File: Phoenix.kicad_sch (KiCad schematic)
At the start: 2 parts

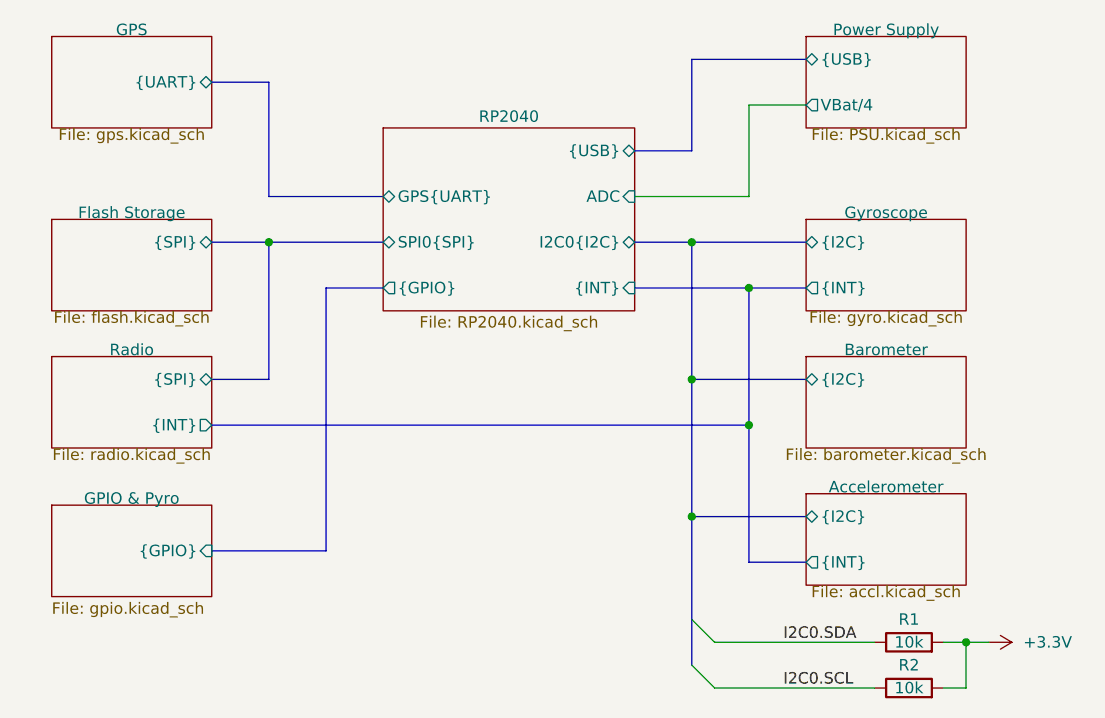
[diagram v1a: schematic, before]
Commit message: Connected the sensors, flash chip, Need to connect the radio and GPS
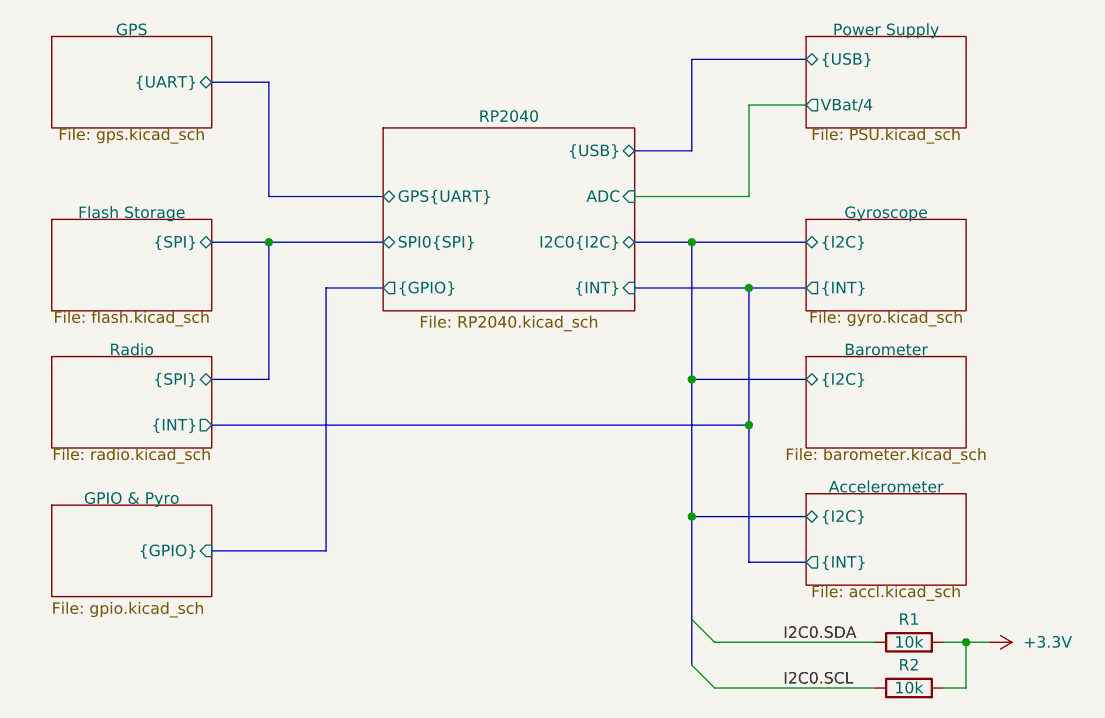
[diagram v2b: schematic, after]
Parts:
- R1, R2: footprint (none) -> Resistor_SMD:R_0603_1608Metric

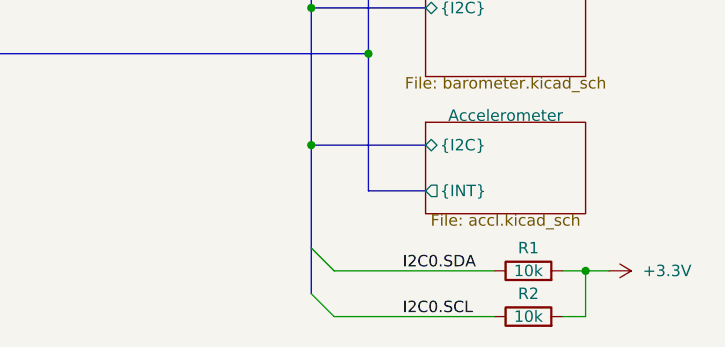
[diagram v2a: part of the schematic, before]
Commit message: Rearranged IO pins to make routing easier. Removed reset, changed BOOTSEL to button
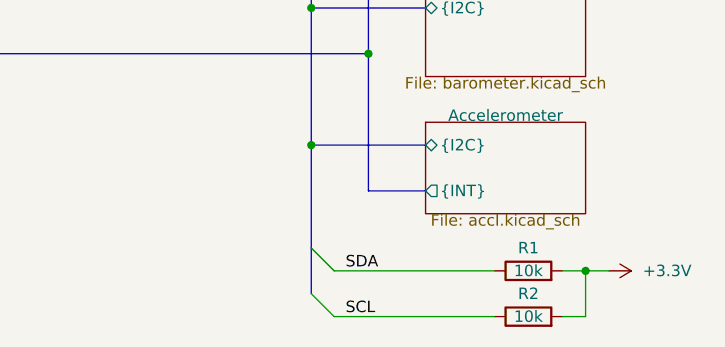
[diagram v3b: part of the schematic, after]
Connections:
- net I2C0.SCL renamed SCL
- net I2C0.SDA renamed SDA
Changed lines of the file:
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@@
   (junction (at 153.67 104.14) (diameter 0) (color 0 0 0 0)
   )
-  (bus_entry (at 125.73 104.14) (size -2.54 -2.54)
-    (stroke (width 0) (type default) (color 0 0 0 0))
-  )
-  (bus_entry (at 125.73 109.22) (size -2.54 -2.54)
+  (bus_entry (at 123.19 101.6) (size 2.54 2.54)
+    (stroke (width 0) (type default) (color 0 0 0 0))
+  )
+  (bus_entry (at 123.19 106.68) (size 2.54 2.54)
     (stroke (width 0) (type default) (color 0 0 0 0))
   )
@@
     (stroke (width 0) (type default) (color 0 0 0 0))
   )
+  (bus (pts (xy 69.85 59.69) (xy 76.2 59.69))
+    (stroke (width 0) (type default) (color 0 0 0 0))
+  )
+  (bus (pts (xy 123.19 49.53) (xy 123.19 39.37))
+    (stroke (width 0) (type default) (color 0 0 0 0))
+  )
+  (wire (pts (xy 153.67 109.22) (xy 151.13 109.22))
+    (stroke (width 0) (type default) (color 0 0 0 0))
+  )
+  (wire (pts (xy 116.84 54.61) (xy 129.54 54.61))
+    (stroke (width 0) (type default) (color 0 0 0 0))
+  )
+  (wire (pts (xy 151.13 104.14) (xy 153.67 104.14))
+    (stroke (width 0) (type default) (color 0 0 0 0))
+  )
+  (bus (pts (xy 76.2 54.61) (xy 88.9 54.61))
+    (stroke (width 0) (type default) (color 0 0 0 0))
+  )
+  (bus (pts (xy 69.85 93.98) (xy 82.55 93.98))
+    (stroke (width 0) (type default) (color 0 0 0 0))
+  )
+  (bus (pts (xy 123.19 39.37) (xy 135.89 39.37))
+    (stroke (width 0) (type default) (color 0 0 0 0))
+  )
+  (wire (pts (xy 153.67 104.14) (xy 156.21 104.14))
+    (stroke (width 0) (type default) (color 0 0 0 0))
+  )
+  (bus (pts (xy 129.54 64.77) (xy 135.89 64.77))
+    (stroke (width 0) (type default) (color 0 0 0 0))
+  )
+  (bus (pts (xy 69.85 74.93) (xy 76.2 74.93))
+    (stroke (width 0) (type default) (color 0 0 0 0))
+  )
+  (wire (pts (xy 125.73 109.22) (xy 143.51 109.22))
+    (stroke (width 0) (type default) (color 0 0 0 0))
+  )
+  (bus (pts (xy 116.84 59.69) (xy 123.19 59.69))
+    (stroke (width 0) (type default) (color 0 0 0 0))
+  )
+  (bus (pts (xy 123.19 59.69) (xy 135.89 59.69))
+    (stroke (width 0) (type default) (color 0 0 0 0))
+  )
+  (bus (pts (xy 123.19 90.17) (xy 135.89 90.17))
+    (stroke (width 0) (type default) (color 0 0 0 0))
+  )
+  (bus (pts (xy 116.84 49.53) (xy 123.19 49.53))
+    (stroke (width 0) (type default) (color 0 0 0 0))
+  )
+  (bus (pts (xy 76.2 59.69) (xy 76.2 74.93))
+    (stroke (width 0) (type default) (color 0 0 0 0))
+  )
+  (bus (pts (xy 116.84 64.77) (xy 129.54 64.77))
+    (stroke (width 0) (type default) (color 0 0 0 0))
+  )
   (wire (pts (xy 125.73 104.14) (xy 143.51 104.14))
     (stroke (width 0) (type default) (color 0 0 0 0))
   )
-  (bus (pts (xy 69.85 59.69) (xy 76.2 59.69))
-    (stroke (width 0) (type default) (color 0 0 0 0))
-  )
-  (bus (pts (xy 123.19 49.53) (xy 123.19 39.37))
-    (stroke (width 0) (type default) (color 0 0 0 0))
-  )
-  (wire (pts (xy 153.67 109.22) (xy 151.13 109.22))
-    (stroke (width 0) (type default) (color 0 0 0 0))
-  )
-  (wire (pts (xy 116.84 54.61) (xy 129.54 54.61))
-    (stroke (width 0) (type default) (color 0 0 0 0))
-  )
-  (wire (pts (xy 151.13 104.14) (xy 153.67 104.14))
-    (stroke (width 0) (type default) (color 0 0 0 0))
-  )
-  (bus (pts (xy 76.2 54.61) (xy 88.9 54.61))
-    (stroke (width 0) (type default) (color 0 0 0 0))
-  )
-  (bus (pts (xy 69.85 93.98) (xy 82.55 93.98))
-    (stroke (width 0) (type default) (color 0 0 0 0))
-  )
-  (bus (pts (xy 123.19 39.37) (xy 135.89 39.37))
+  (bus (pts (xy 82.55 64.77) (xy 88.9 64.77))
+    (stroke (width 0) (type default) (color 0 0 0 0))
+  )
+  (bus (pts (xy 123.19 74.93) (xy 135.89 74.93))
+    (stroke (width 0) (type default) (color 0 0 0 0))
+  )
+  (bus (pts (xy 123.19 59.69) (xy 123.19 74.93))
+    (stroke (width 0) (type default) (color 0 0 0 0))
+  )
+  (bus (pts (xy 76.2 59.69) (xy 88.9 59.69))
+    (stroke (width 0) (type default) (color 0 0 0 0))
+  )
+  (bus (pts (xy 129.54 64.77) (xy 129.54 80.01))
+    (stroke (width 0) (type default) (color 0 0 0 0))
+  )
+  (bus (pts (xy 123.19 74.93) (xy 123.19 90.17))
+    (stroke (width 0) (type default) (color 0 0 0 0))
+  )
+  (bus (pts (xy 82.55 64.77) (xy 82.55 93.98))
     (stroke (width 0) (type default) (color 0 0 0 0))
   )
@@
     (stroke (width 0) (type default) (color 0 0 0 0))
   )
-  (wire (pts (xy 153.67 104.14) (xy 156.21 104.14))
-    (stroke (width 0) (type default) (color 0 0 0 0))
-  )
-  (bus (pts (xy 129.54 64.77) (xy 135.89 64.77))
-    (stroke (width 0) (type default) (color 0 0 0 0))
-  )
-  (bus (pts (xy 69.85 74.93) (xy 76.2 74.93))
-    (stroke (width 0) (type default) (color 0 0 0 0))
-  )
-  (wire (pts (xy 125.73 109.22) (xy 143.51 109.22))
-    (stroke (width 0) (type default) (color 0 0 0 0))
-  )
-  (bus (pts (xy 116.84 59.69) (xy 123.19 59.69))
-    (stroke (width 0) (type default) (color 0 0 0 0))
-  )
-  (bus (pts (xy 123.19 59.69) (xy 135.89 59.69))
-    (stroke (width 0) (type default) (color 0 0 0 0))
-  )
-  (bus (pts (xy 123.19 90.17) (xy 135.89 90.17))
-    (stroke (width 0) (type default) (color 0 0 0 0))
-  )
-  (bus (pts (xy 116.84 49.53) (xy 123.19 49.53))
-    (stroke (width 0) (type default) (color 0 0 0 0))
-  )
-  (bus (pts (xy 76.2 59.69) (xy 76.2 74.93))
-    (stroke (width 0) (type default) (color 0 0 0 0))
-  )
-  (bus (pts (xy 116.84 64.77) (xy 129.54 64.77))
-    (stroke (width 0) (type default) (color 0 0 0 0))
-  )
-  (bus (pts (xy 82.55 64.77) (xy 88.9 64.77))
-    (stroke (width 0) (type default) (color 0 0 0 0))
-  )
-  (bus (pts (xy 123.19 74.93) (xy 135.89 74.93))
-    (stroke (width 0) (type default) (color 0 0 0 0))
-  )
-  (bus (pts (xy 123.19 59.69) (xy 123.19 74.93))
-    (stroke (width 0) (type default) (color 0 0 0 0))
-  )
-  (bus (pts (xy 76.2 59.69) (xy 88.9 59.69))
-    (stroke (width 0) (type default) (color 0 0 0 0))
-  )
-  (bus (pts (xy 129.54 64.77) (xy 129.54 80.01))
-    (stroke (width 0) (type default) (color 0 0 0 0))
-  )
-  (bus (pts (xy 123.19 74.93) (xy 123.19 90.17))
-    (stroke (width 0) (type default) (color 0 0 0 0))
-  )
-  (bus (pts (xy 82.55 64.77) (xy 82.55 93.98))
-    (stroke (width 0) (type default) (color 0 0 0 0))
-  )
   (wire (pts (xy 153.67 104.14) (xy 153.67 109.22))
     (stroke (width 0) (type default) (color 0 0 0 0))
@@
     (stroke (width 0) (type default) (color 0 0 0 0))
   )
-  (label "I2C0.SCL" (at 133.35 109.22 0)
+  (label "SCL" (at 127 109.22 0)
     (effects (font (size 1.27 1.27)) (justify left bottom))
   )
-  (label "I2C0.SDA" (at 133.35 104.14 0)
+  (label "SDA" (at 127 104.14 0)
     (effects (font (size 1.27 1.27)) (justify left bottom))
   )
@@
       (reference "#PWR02") (unit 1) (value "+3.3V") (footprint "")
     )
-    (path "/973e92e2-e415-4dc5-9283-1d2d8aa34625/6d0fc5b1-9c2a-4a32-828c-96b4f7e43a4d"
-      (reference "#PWR03") (unit 1) (value "GND") (footprint "")
-    )
     (path "/973e92e2-e415-4dc5-9283-1d2d8aa34625/0ca807b9-ec9b-4f8f-847e-6bace1eb03e3"
       (reference "#PWR04") (unit 1) (value "+1V1") (footprint "")
@@
       (reference "#PWR07") (unit 1) (value "+3.3V") (footprint "")
     )
-    (path "/973e92e2-e415-4dc5-9283-1d2d8aa34625/dba47cb0-c726-4b08-99cb-d5e815061e25"
-      (reference "#PWR08") (unit 1) (value "+3.3V") (footprint "")
-    )
     (path "/973e92e2-e415-4dc5-9283-1d2d8aa34625/7c70c5b5-8ba3-46e5-a95a-19d470115de7"
       (reference "#PWR09") (unit 1) (value "+1V1") (footprint "")
@@
       (reference "J5") (unit 1) (value "Conn_01x05_Male") (footprint "")
     )
-    (path "/973e92e2-e415-4dc5-9283-1d2d8aa34625/0111ad60-beec-4fdd-bf52-89c00a0b04af"
-      (reference "JP1") (unit 1) (value "RESET") (footprint "Jumper:SolderJumper-2_P1.3mm_Open_RoundedPad1.0x1.5mm")
-    )
     (path "/973e92e2-e415-4dc5-9283-1d2d8aa34625/c47b14a7-f4aa-44aa-bba9-bf0e2945fed9"
-      (reference "JP2") (unit 1) (value "BOOTSEL") (footprint "Jumper:SolderJumper-2_P1.3mm_Open_RoundedPad1.0x1.5mm")
+      (reference "JP2") (unit 1) (value "BOOTSEL") (footprint "Button_Switch_SMD:SW_SPST_B3U-1000P")
     )
     (path "/0ac888d5-4182-4a88-8f62-40ce12e3896a/17f147e3-c667-41bb-89e2-ef95a3c7390b"
@@
       (reference "R2") (unit 1) (value "10k") (footprint "Resistor_SMD:R_0603_1608Metric")
     )
-    (path "/973e92e2-e415-4dc5-9283-1d2d8aa34625/188666a7-1177-4a1d-80f2-6f38040ebc89"
-      (reference "R3") (unit 1) (value "1k") (footprint "Resistor_SMD:R_0603_1608Metric")
-    )
     (path "/973e92e2-e415-4dc5-9283-1d2d8aa34625/365d1fd1-547e-42e3-ad75-f7c0cd8d8a12"
       (reference "R4") (unit 1) (value "27") (footprint "Resistor_SMD:R_0603_1608Metric_Pad0.98x0.95mm_HandSolder")
@@
       (reference "R5") (unit 1) (value "27") (footprint "Resistor_SMD:R_0603_1608Metric_Pad0.98x0.95mm_HandSolder")
     )
-    (path "/973e92e2-e415-4dc5-9283-1d2d8aa34625/02d36bad-0ed7-46a4-a32a-bfcf65aff319"
-      (reference "R6") (unit 1) (value "10k") (footprint "Resistor_SMD:R_0603_1608Metric")
-    )
-    (path "/973e92e2-e415-4dc5-9283-1d2d8aa34625/843072f6-cf10-4bdf-9d28-cf384259e0ef"
-      (reference "R7") (unit 1) (value "10k") (footprint "Resistor_SMD:R_0603_1608Metric")
-    )
     (path "/973e92e2-e415-4dc5-9283-1d2d8aa34625/7239285e-3faf-4ba7-895f-832ed4958cbd"
